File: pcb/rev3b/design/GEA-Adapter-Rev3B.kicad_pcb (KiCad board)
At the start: 4 copper layers, 99 x 40 mm, 99 parts, among them J1 8P8C, J2 RECOVERY, Q3 CJ3407, Q4 CJ3407, Q5 MMBT3904, U10 TPS22810DBVR, U2 XIAO ESP32-C3 v1.3 (22-pad), U4 74LVC2G07, U5 74LVC2G07_3v3, U8 AP63205WU, U9 TPS22810DBVR

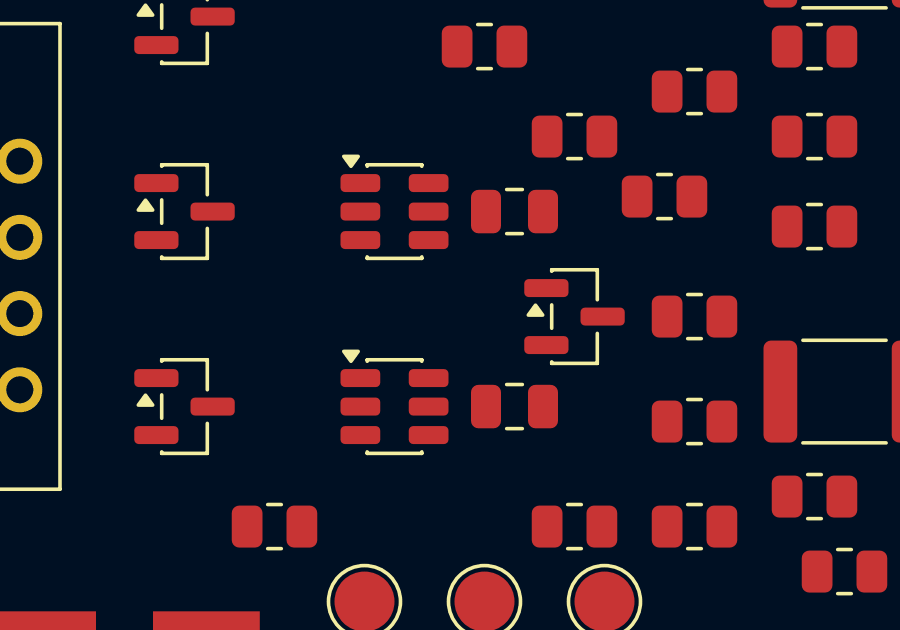
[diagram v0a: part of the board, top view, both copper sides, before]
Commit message: fix(pcb): secure Rev3B buffer supply and ground returns
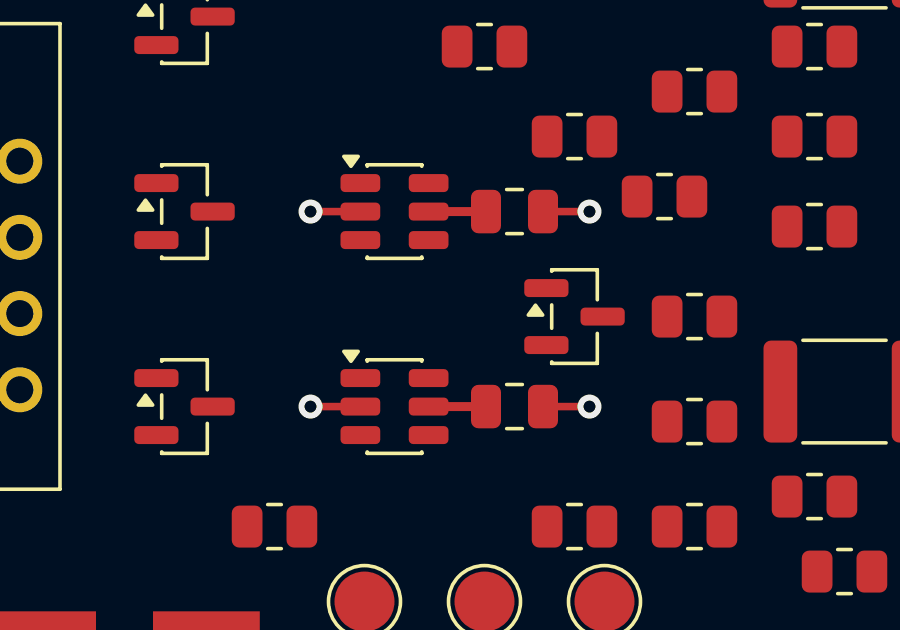
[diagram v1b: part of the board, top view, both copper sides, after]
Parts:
- turned C4 to 180 degrees
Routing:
- net GND: track 27.3 -> 33.7 mm, vias 12 -> 16
- net +5V: track 9.81 -> 11.7 mm
- net +3V3: track 0.00 -> 1.91 mm
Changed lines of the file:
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@@
 	(footprint "Capacitor_SMD:C_0805_2012Metric"
 		(layer "F.Cu")
-		(at 33 22)
+		(at 33 22 180)
 		(descr "Capacitor SMD 0805 (2012 Metric), square (rectangular) end terminal, IPC-7351 nominal, (Body size source: IPC-SM-782 page 76, https://www.pcb-3d.com/wordpress/wp-content/uploads/ipc-sm-782a_amendment_1_and_2.pdf, https://docs.google.com/spreadsheets/d/1BsfQQcO9C6DZCsRaXUlFlo91Tg2WpOkGARC1WS5S8t0/edit?usp=sharing), generated with kicad-footprint-generator")
 		(tags "capacitor")
 		(property "Reference" "C4"
-			(at 0 -1.68 0)
+			(at 0 -1.68 180)
 			(layer "F.Fab")
 			(effects
@@
 		)
 		(property "Value" "100n"
-			(at 0 1.68 0)
+			(at 0 1.68 180)
 			(layer "F.Fab")
 			(hide yes)
@@
 		)
 		(property "Datasheet" "~"
-			(at 0 0 0)
+			(at 0 0 180)
 			(layer "F.Fab")
 			(hide yes)
@@
 		)
 		(property "Description" "C106243"
-			(at 0 0 0)
+			(at 0 0 180)
 			(layer "F.Fab")
 			(hide yes)
@@
 		)
 		(property "LCSC" "C106243"
-			(at 0 0 0)
+			(at 0 0 180)
 			(layer "F.Fab")
 			(hide yes)
@@
 		(attr smd)
 		(fp_line
-			(start -0.261252 -0.735)
-			(end 0.261252 -0.735)
+			(start -0.261252 0.735)
+			(end 0.261252 0.735)
 			(stroke
 				(width 0.12)
@@
 		)
 		(fp_line
-			(start -0.261252 0.735)
-			(end 0.261252 0.735)
+			(start -0.261252 -0.735)
+			(end 0.261252 -0.735)
 			(stroke
 				(width 0.12)
@@
 		)
 		(fp_text user "${REFERENCE}"
-			(at 0 0 0)
+			(at 0 0 180)
 			(layer "F.Fab")
 			(effects
@@
 		)
 		(pad "1" smd roundrect
-			(at -0.95 0)
+			(at -0.95 0 180)
 			(size 1 1.45)
 			(layers "F.Cu" "F.Mask" "F.Paste")
@@
 		)
 		(pad "2" smd roundrect
-			(at 0.95 0)
+			(at 0.95 0 180)
 			(size 1 1.45)
 			(layers "F.Cu" "F.Mask" "F.Paste")
@@
 	)
 	(segment
+		(start 30.1375 22)
+		(end 32.05 22)
+		(width 0.3)
+		(layer "F.Cu")
+		(net 1)
+	)
+	(segment
+		(start 30.1375 15.5)
+		(end 32.05 15.5)
+		(width 0.3)
+		(layer "F.Cu")
+		(net 2)
+	)
+	(segment
 		(start 74.6 37)
 		(end 72.7 38)
@@
 	)
 	(segment
+		(start 33.95 15.5)
+		(end 35.5 15.5)
+		(width 0.25)
+		(layer "F.Cu")
+		(net 14)
+	)
+	(segment
+		(start 33.95 22)
+		(end 35.5 22)
+		(width 0.25)
+		(layer "F.Cu")
+		(net 14)
+	)
+	(segment
+		(start 27.8625 15.5)
+		(end 26.2 15.5)
+		(width 0.25)
+		(layer "F.Cu")
+		(net 14)
+	)
+	(segment
 		(start 68.95 21.5)
 		(end 69.8 20)
@@
 	)
 	(segment
+		(start 27.8625 22)
+		(end 26.2 22)
+		(width 0.25)
+		(layer "F.Cu")
+		(net 14)
+	)
+	(segment
 		(start 61.6 24.7)
 		(end 61.65 24.7)
@@
 	)
 	(via
+		(at 35.5 22)
+		(size 0.8)
+		(drill 0.4)
+		(layers "F.Cu" "B.Cu")
+		(net 14)
+	)
+	(via
+		(at 35.5 15.5)
+		(size 0.8)
+		(drill 0.4)
+		(layers "F.Cu" "B.Cu")
+		(net 14)
+	)
+	(via
+		(at 26.2 15.5)
+		(size 0.8)
+		(drill 0.4)
+		(layers "F.Cu" "B.Cu")
+		(net 14)
+	)
+	(via
 		(at 69.8 20)
 		(size 0.8)
@@
 		(size 0.8)
 		(drill 0.4)
+		(layers "F.Cu" "B.Cu")
+		(net 14)
+	)
+	(via
+		(at 26.2 22)
+		(size 0.8)
+		(drill 0.4)

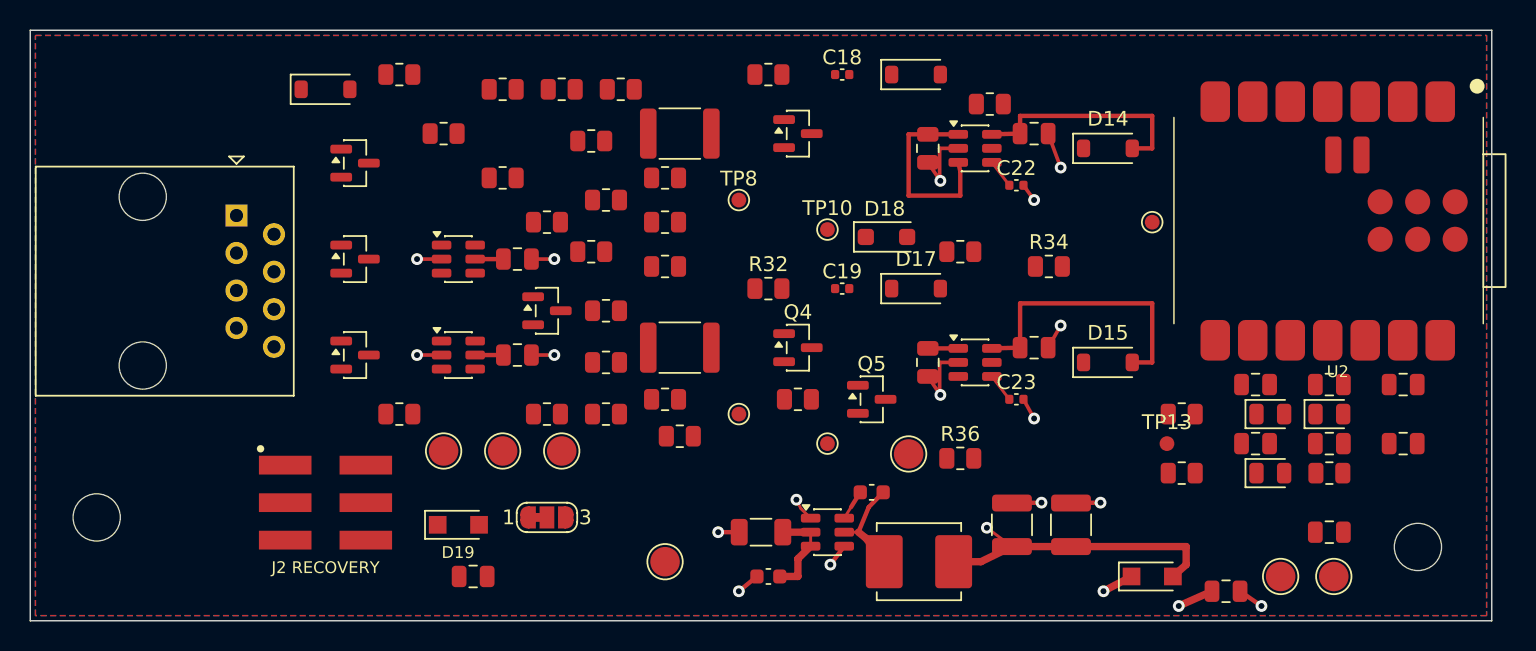
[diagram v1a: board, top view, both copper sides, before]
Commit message: feat(pcb): complete Rev3B four-layer routing
Connect the remaining power and signal nets, stitch ground pours, and orient the RJ45 ground thermal relief to preserve two spokes. Retain the local buck and selector routes, 0.2 mm minimum tracks, and ordinary 0.8/0.4 mm vias.
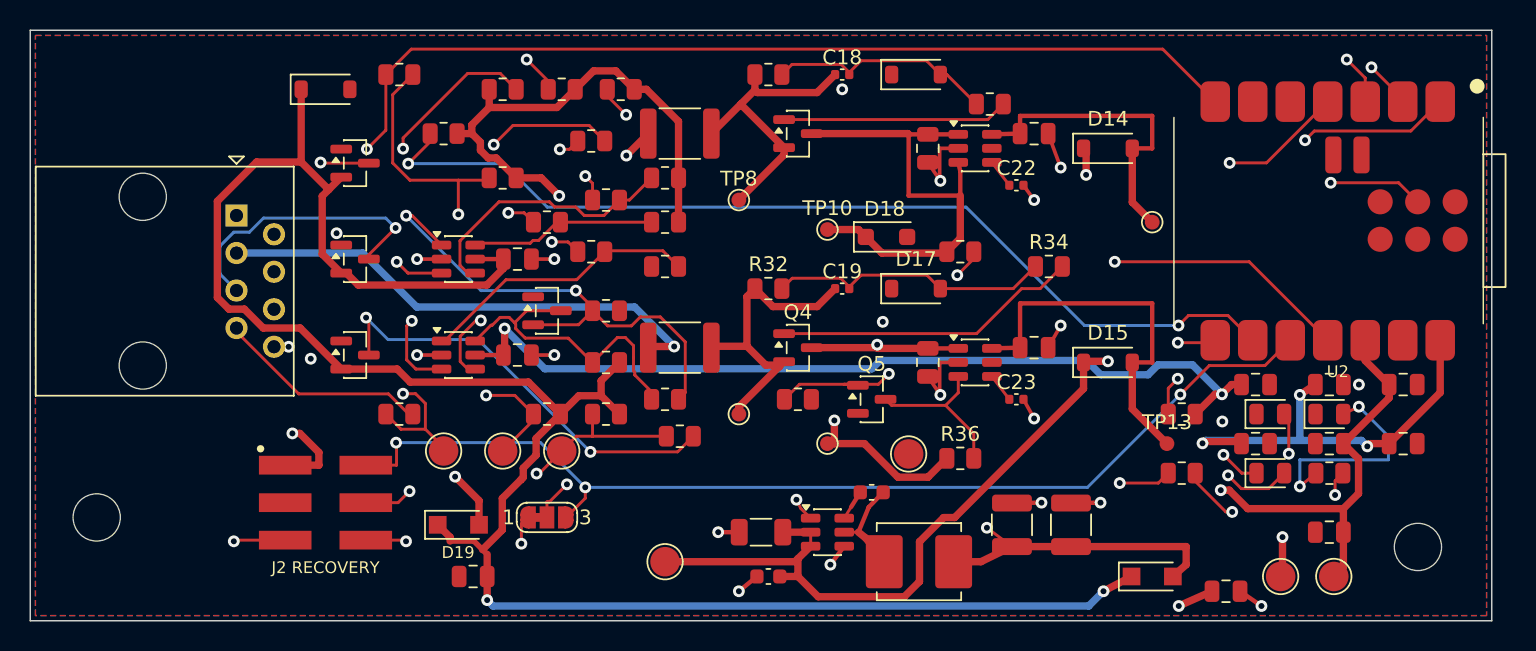
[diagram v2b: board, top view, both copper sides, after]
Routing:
- net +5V: track 11.7 -> 196.8 mm, vias 2 -> 7
- net +3V3: track 1.91 -> 140.4 mm, vias 0 -> 4
- net EN: track 0.00 -> 119.9 mm, vias 0 -> 3
- net BOOT: track 0.00 -> 103.5 mm, vias 0 -> 4
- net GEA3_RX: track 0.00 -> 98.9 mm, vias 0 -> 2
- net GEA3_TX: track 0.00 -> 93.5 mm, vias 0 -> 3
- net /DBG_LED: track 0.00 -> 85.5 mm, vias 0 -> 3
- net /GEA2_MCU_TX: track 0.00 -> 72.7 mm, vias 0 -> 2
- net /BOOT_SEL: track 0.00 -> 65.4 mm, vias 0 -> 2
- net GEA2_RX: track 0.00 -> 63.7 mm, vias 0 -> 2
- net Net-(D9-K2): track 0.00 -> 56.9 mm, vias 0 -> 3
- net /V_INPUT: track 6.47 -> 62.6 mm, vias 0 -> 2
- net /LED2: track 0.00 -> 48.0 mm, vias 0 -> 2
- net GEA_FullTx: track 0.00 -> 45.3 mm, vias 0 -> 2
- net /LED1: track 0.00 -> 38.3 mm, vias 0 -> 2
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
